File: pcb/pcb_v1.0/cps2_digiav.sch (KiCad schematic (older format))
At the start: 47 parts, among them U31 74LVC245, U32 74LVC245, U33 74LVC245, U34 SN74LVC3G17, U7 TC1262-3.3VDBTR, U8 TLV70033

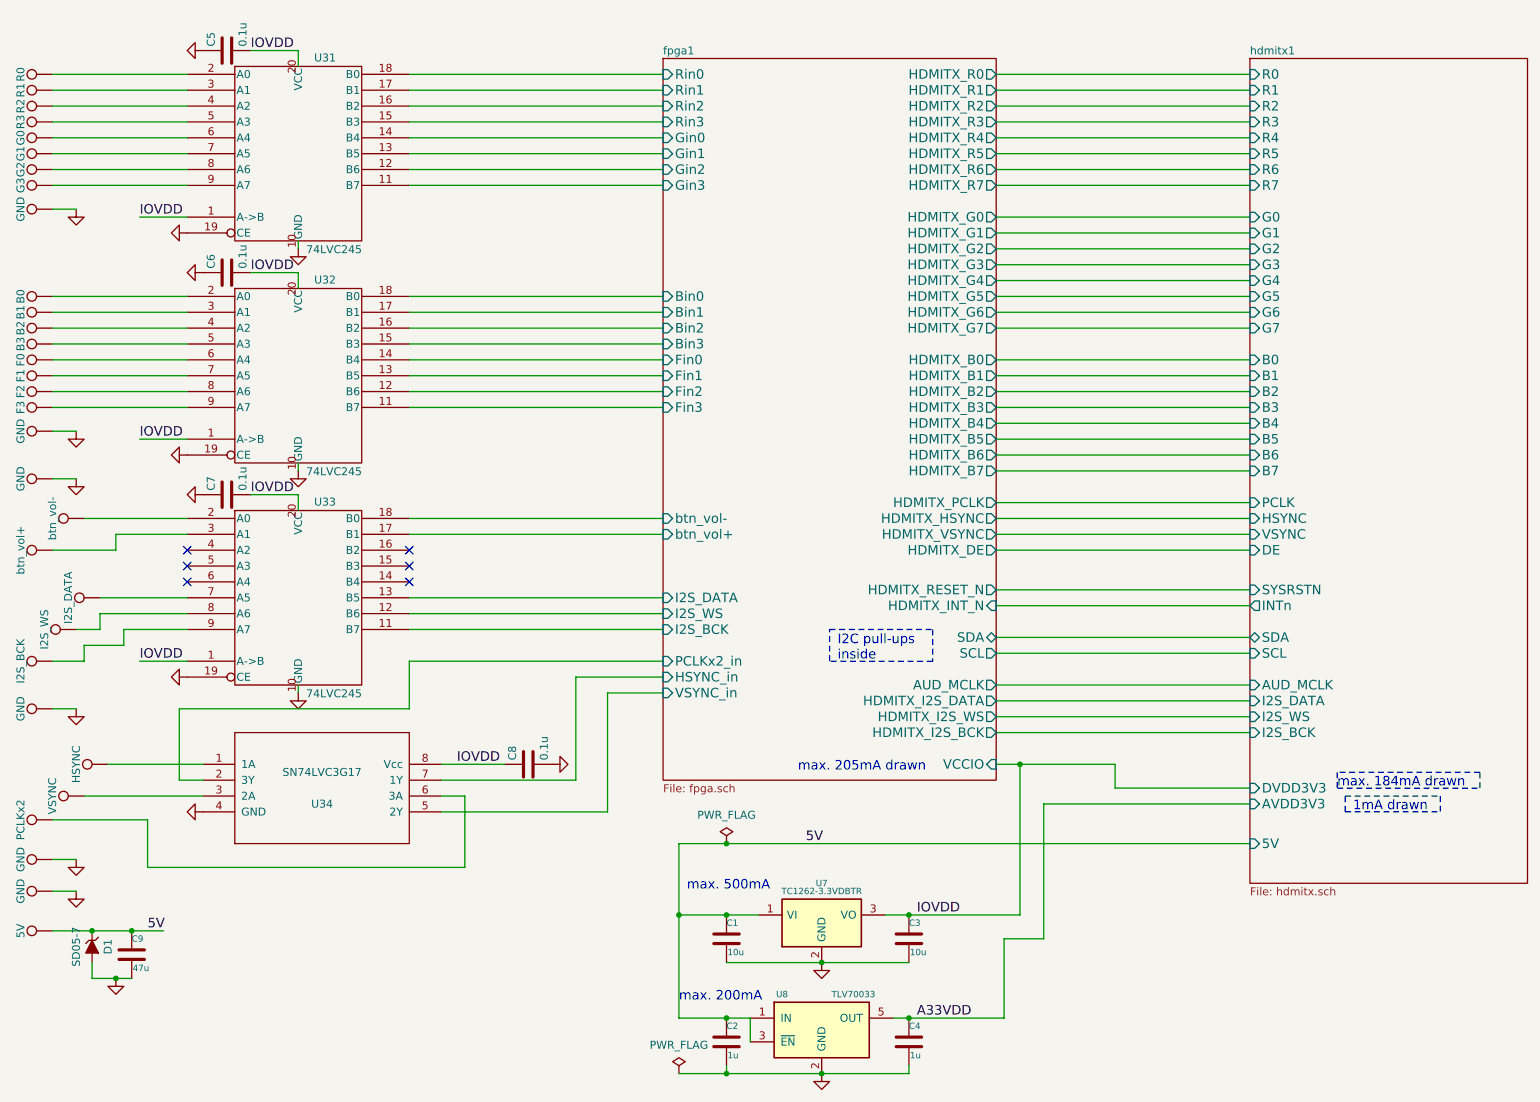
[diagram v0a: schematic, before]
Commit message: This is a combination of 10 commits.
Moved ICs to top, made to fit ontop of CPS2 DIPs

Added ADV7513

update lib path

Finished power section of ADV7531

initial layout of ADV7513

Added Si5351C

Reordered inputs, improved clock layout

Final changes before pull req

Removing auto-generated files

Removing remaining auto-generated files
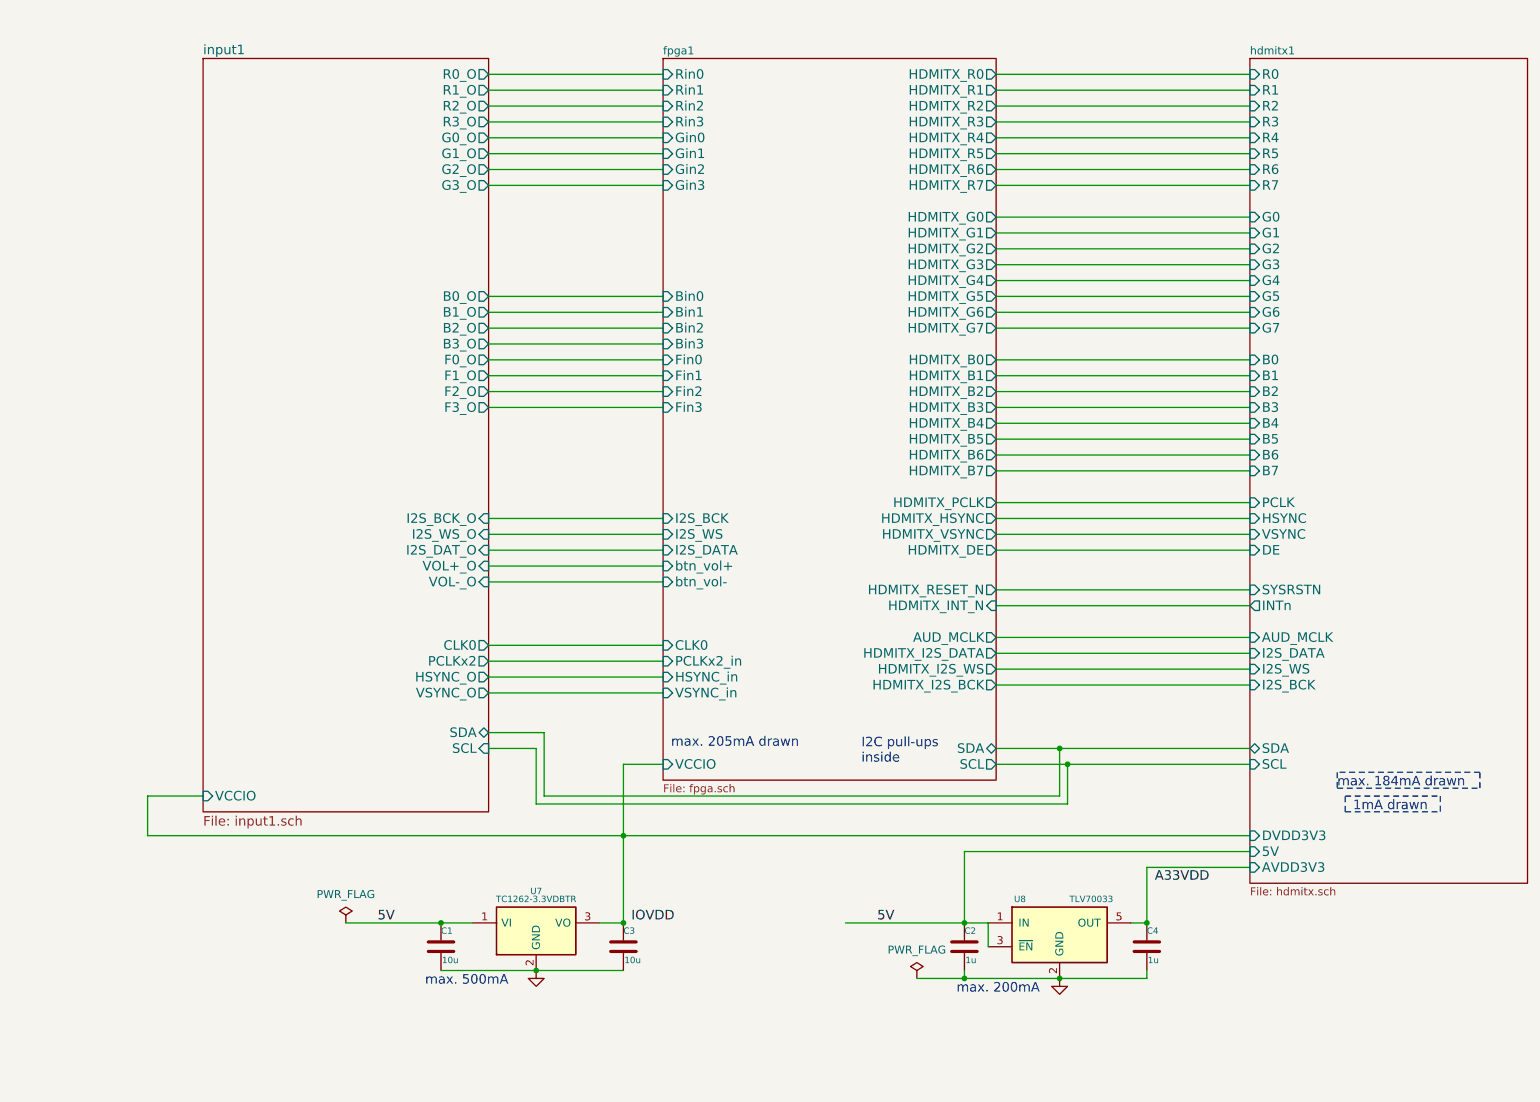
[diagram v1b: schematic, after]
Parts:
- removed C5, C6, C7, C8: 0.1u, custom_components:SM0603_Capa_libcms, symbol C
- removed C9: 47u, custom_components:SM0603_Capa_libcms, symbol C
- removed D1: SD05-7, custom_components:SOD-323_Handsoldering, symbol ZENERsmall
- removed U31, U32, U33: 74LVC245, custom_components:TSSOP-20_4.4x6.5mm_Pitch0.65mm_Handsoldering, symbol 74LVC245
- removed U34: SN74LVC3G17, custom_components:SSOP-8_3x3mm_Pitch0.65mm, symbol SN74LVC3G17
- removed W1: 5V, custom_components:SMD_PAD, symbol TEST_1P
- removed W10: G3, custom_components:SMD_PAD, symbol TEST_1P
- removed W11: B0, custom_components:SMD_PAD, symbol TEST_1P
- removed W12: B1, custom_components:SMD_PAD, symbol TEST_1P
- removed W13: B2, custom_components:SMD_PAD, symbol TEST_1P
- removed W14: B3, custom_components:SMD_PAD, symbol TEST_1P
- removed W15: F0, custom_components:SMD_PAD, symbol TEST_1P
- removed W16: F1, custom_components:SMD_PAD, symbol TEST_1P
- removed W17: F2, custom_components:SMD_PAD, symbol TEST_1P
- removed W18: F3, custom_components:SMD_PAD, symbol TEST_1P
- removed W19: btn_vol+, custom_components:SMD_PAD, symbol TEST_1P
- removed W2, W27, W28, W29, W30, W31: GND, custom_components:SMD_PAD, symbol TEST_1P
- removed W20: I2S_BCK, custom_components:SMD_PAD, symbol TEST_1P
- removed W21: PCLKx2, custom_components:SMD_PAD, symbol TEST_1P
- removed W22: I2S_WS, custom_components:SMD_PAD, symbol TEST_1P
- removed W23: btn_vol-, custom_components:SMD_PAD, symbol TEST_1P
- removed W24: VSYNC, custom_components:SMD_PAD, symbol TEST_1P
- removed W25: I2S_DATA, custom_components:SMD_PAD, symbol TEST_1P
- removed W26: HSYNC, custom_components:SMD_PAD, symbol TEST_1P
- removed W3: R0, custom_components:SMD_PAD, symbol TEST_1P
- removed W4: R1, custom_components:SMD_PAD, symbol TEST_1P
- removed W5: R2, custom_components:SMD_PAD, symbol TEST_1P
- removed W6: R3, custom_components:SMD_PAD, symbol TEST_1P
- removed W7: G0, custom_components:SMD_PAD, symbol TEST_1P
- removed W8: G1, custom_components:SMD_PAD, symbol TEST_1P
- removed W9: G2, custom_components:SMD_PAD, symbol TEST_1P
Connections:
- net A33VDD: no longer C4.1, U8.5 (OUT)
- net IOVDD: no longer C3.1, U7.3 (VO)
- new net fpga1/VCCIO: C3.1, U7.3 (VO)
- new net hdmitx1/AVDD3V3: C4.1, U8.5 (OUT)
- no-connect marks 6 -> 0
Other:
- moved on the sheet: C1, C2, C3, C4, U7, U8

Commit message: fix schematic and library linkage issues
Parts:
- U7: value TC1262-3.3VDBTR -> AP7361; symbol SPX2920M3-3.3 -> TC1262-33
- U8: symbol TLV71209DBV -> TLV70033_SOT23-5
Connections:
- wire segments 87 -> 89
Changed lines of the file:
@@
 LIBS:valves
 LIBS:custom_components
-LIBS:74lvc
-LIBS:altera
-LIBS:analog_devices
-LIBS:barrel_jack
-LIBS:battery
-LIBS:beaglebone_black
-LIBS:ck
-LIBS:conn_power
-LIBS:conn_rf
-LIBS:conn_rj
-LIBS:crystal
-LIBS:ddr2_sdram_sodimm
-LIBS:diode
-LIBS:epcos
-LIBS:epcos_dcc6c
-LIBS:fbead
-LIBS:fiducial
-LIBS:freescale_mcu
-LIBS:hackrf_expansion
-LIBS:hdmi
-LIBS:header
-LIBS:hirose
-LIBS:hole
-LIBS:io_expander
-LIBS:lcd_kingtech
-LIBS:ltc
-LIBS:microphone
-LIBS:minicircuits
-LIBS:molex
-LIBS:mosfet
-LIBS:newhaven
-LIBS:noritake
-LIBS:nxp_micro
-LIBS:on_cat24c256
-LIBS:on_semi
-LIBS:osc
-LIBS:passive
-LIBS:regulator
-LIBS:rf_antenna
-LIBS:rf_lna
-LIBS:r_sense
-LIBS:samtec
-LIBS:sd
-LIBS:sharebrained
-LIBS:silabs
-LIBS:supply
-LIBS:switch
-LIBS:terminal_block
-LIBS:ti
-LIBS:ti_cc
-LIBS:tp
-LIBS:trs_jack
-LIBS:usb3_esd_son50-10
-LIBS:usb3_micro_ab
-LIBS:wolfson
-LIBS:ossc_board-cache
+LIBS:HDMI
 LIBS:cps2_digiav-cache
 EELAYER 25 0
@@
 Title "CPS2_digiAV"
 Date "2016-09-24"
-Rev "1.0"
+Rev "2.0"
 Comp ""
 Comment1 ""
@@
 F40 "I2S_BCK" I L 8350 5150 60
 $EndSheet
-Text Label 7750 6400 0    60   ~ 0
+Text Label 7750 6300 0    60   ~ 0
 A33VDD
 Text Label 4450 6650 0    60   ~ 0
 IOVDD
 $Comp
-L TLV71209DBV U8
+L TLV70033_SOT23-5 U8
 U 1 1 57E7546E
 P 7150 6700
@@
 max. 500mA
 $Comp
-L SPX2920M3-3.3 U7
+L TC1262-33 U7
 U 1 1 57E754A0
-P 3850 6700
-F 0 "U7" H 3850 6950 40  0000 C CNN
-F 1 "TC1262-3.3VDBTR" H 3850 6900 40  0000 C CNN
-F 2 "custom_components:SOT-223_Handsoldering" H 3850 6800 35  0001 C CIN
-F 3 "" H 3850 6700 60  0000 C CNN
-	1    3850 6700
+P 3850 6650
+F 0 "U7" H 3850 6850 40  0000 C CNN
+F 1 "AP7361" H 3850 6800 40  0000 C CNN
+F 2 "custom_components:SOT-223_Handsoldering" H 3850 6750 35  0001 C CIN
+F 3 "" H 3850 6650 60  0000 C CNN
+	1    3850 6650
 	1    0    0    -1
 $EndComp
@@
 Connection ~ 6550 6650
 Wire Wire Line
-	5800 6650 6700 6650
-Wire Wire Line
-	6700 6650 6700 6800
+	5800 6650 6850 6650
 Connection ~ 3250 6650
 Connection ~ 4400 6650
@@
 	3550 3400 4650 3400
 Wire Wire Line
-	2650 6650 3450 6650
+	2650 6650 3550 6650
 Connection ~ 7700 6650
 Wire Wire Line
@@
 	6750 5150 8350 5150
 Wire Wire Line
-	4400 6650 4250 6650
+	4400 6650 4150 6650
 Connection ~ 4400 6100
 Wire Wire Line
@@
 Wire Wire Line
 	3550 4900 4650 4900
+Wire Wire Line
+	6850 6600 6850 6700
+Connection ~ 6850 6650
+Wire Wire Line
+	7450 6600 7600 6600
+Wire Wire Line
+	7600 6600 7600 6650
 $EndSCHEMATC
